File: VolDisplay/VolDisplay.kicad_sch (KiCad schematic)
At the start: 126 parts, among them J1 TYPE-C-31-M-12, SW1 PTS810_SJM_250_SMTR_LFS, SW2 PTS810_SJM_250_SMTR_LFS, U1 ESP32-S3-WROOM-1, U2 AMS1117-3.3

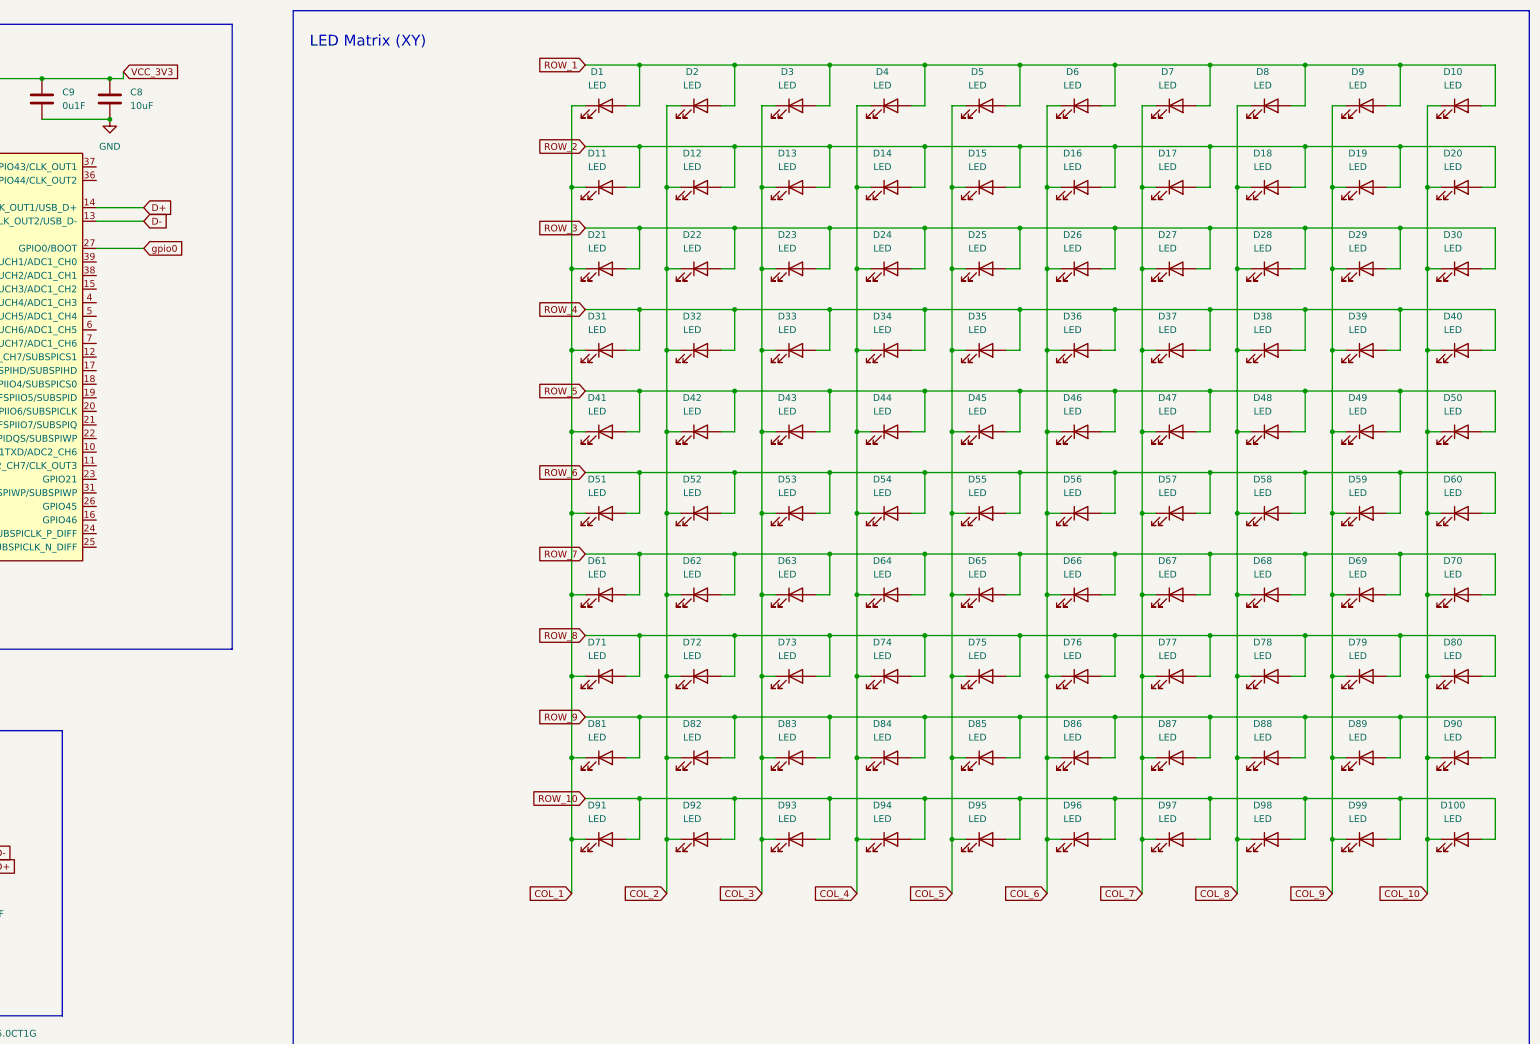
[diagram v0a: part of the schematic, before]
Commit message: Added the automation scripts we used, Schematic PDF is attached.
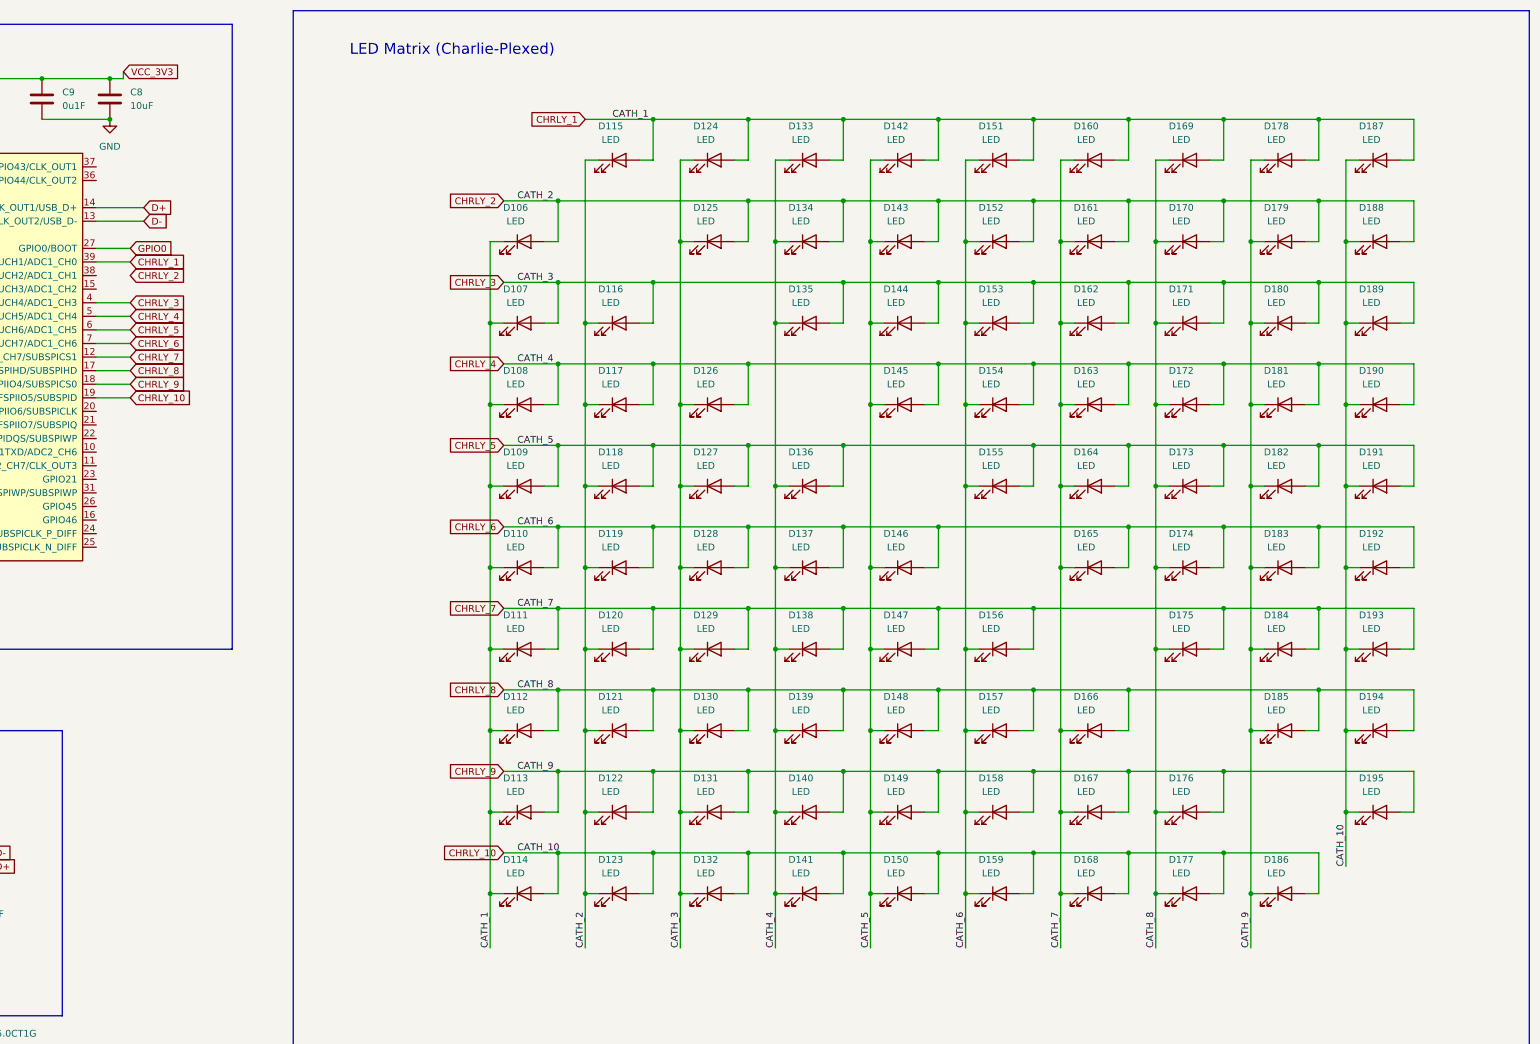
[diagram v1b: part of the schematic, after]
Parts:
- removed D1, D10, D100, D11, D12, D13, D14, D15, D16, D17, D18, D19, D2, D20, D21, D22, D23, D24, D25, D26, D27, D28, D29, D3, D30, D31, D32, D33, D34, D35, D36, D37, D38, D39, D4, D40, D41, D42, D43, D44, D45, D46, D47, D48, D49, D5, D50, D51, D52, D53, D54, D55, D56, D57, D58, D59, D6, D60, D61, D62, D63, D64, D65, D66, D67, D68, D69, D7, D70, D71, D72, D73, D74, D75, D76, D77, D78, D79, D8, D80, D81, D82, D83, D84, D85, D86, D87, D88, D89, D9, D90, D91, D92, D93, D94, D95, D96, D97, D98, D99: LED, LED_SMD:LED_0603_1608Metric_Pad1.05x0.95mm_HandSolder, symbol Device:LED
- added D106, D107, D108, D109, D110, D111, D112, D113, D114, D115, D116, D117, D118, D119, D120, D121, D122, D123, D124, D125, D126, D127, D128, D129, D130, D131, D132, D133, D134, D135, D136, D137, D138, D139, D140, D141, D142, D143, D144, D145, D146, D147, D148, D149, D150, D151, D152, D153, D154, D155, D156, D157, D158, D159, D160, D161, D162, D163, D164, D165, D166, D167, D168, D169, D170, D171, D172, D173, D174, D175, D176, D177, D178, D179, D180, D181, D182, D183, D184, D185, D186, D187, D188, D189, D190, D191, D192, D193, D194, D195: LED, LED_SMD:LED_0201_0603Metric, symbol Device:LED
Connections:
- net gpio0 is gone; now on net GPIO0: U1.27 (GPIO0/BOOT)
- net CHRLY_7: now reaches U1.12 (GPIO8/TOUCH8/ADC1_CH7/SUBSPICS1)
- net CHRLY_7: now also D111.2 (A), D120.2 (A), D129.2 (A), D138.2 (A), D147.2 (A), D156.2 (A), D160.1 (K), D161.1 (K), D162.1 (K), D163.1 (K), D164.1 (K), D165.1 (K), D166.1 (K), D167.1 (K), D168.1 (K), D175.2 (A), D184.2 (A), D193.2 (A)
- net CHRLY_8: now reaches U1.17 (GPIO9/TOUCH9/ADC1_CH8/FSPIHD/SUBSPIHD)
- net CHRLY_8: now also D112.2 (A), D121.2 (A), D130.2 (A), D139.2 (A), D148.2 (A), D157.2 (A), D166.2 (A), D169.1 (K), D170.1 (K), D171.1 (K), D172.1 (K), D173.1 (K), D174.1 (K), D175.1 (K), D176.1 (K), D177.1 (K), D185.2 (A), D194.2 (A)
- net CHRLY_9: now reaches U1.18 (GPIO10/TOUCH10/ADC1_CH9/FSPICS0/FSPIIO4/SUBSPICS0)
- net CHRLY_9: now also D113.2 (A), D122.2 (A), D131.2 (A), D140.2 (A), D149.2 (A), D158.2 (A), D167.2 (A), D176.2 (A), D178.1 (K), D179.1 (K), D180.1 (K), D181.1 (K), D182.1 (K), D183.1 (K), D184.1 (K), D185.1 (K), D186.1 (K), D195.2 (A)
- net CHRLY_10: now reaches U1.19 (GPIO11/TOUCH11/ADC2_CH0/FSPID/FSPIIO5/SUBSPID)
- net CHRLY_10: now also D114.2 (A), D123.2 (A), D132.2 (A), D141.2 (A), D150.2 (A), D159.2 (A), D168.2 (A), D177.2 (A), D186.2 (A), D187.1 (K), D188.1 (K), D189.1 (K), D190.1 (K), D191.1 (K), D192.1 (K), D193.1 (K), D194.1 (K), D195.1 (K)
- net CHRLY_1: now reaches U1.39 (GPIO1/TOUCH1/ADC1_CH0)
- net CHRLY_1: now also D106.1 (K), D107.1 (K), D108.1 (K), D109.1 (K), D110.1 (K), D111.1 (K), D112.1 (K), D113.1 (K), D114.1 (K), D115.2 (A), D124.2 (A), D133.2 (A), D142.2 (A), D151.2 (A), D160.2 (A), D169.2 (A), D178.2 (A), D187.2 (A)
- net CHRLY_3: now reaches U1.4 (GPIO4/TOUCH4/ADC1_CH3)
- net CHRLY_3: now also D107.2 (A), D116.2 (A), D124.1 (K), D125.1 (K), D126.1 (K), D127.1 (K), D128.1 (K), D129.1 (K), D130.1 (K), D131.1 (K), D132.1 (K), D135.2 (A), D144.2 (A), D153.2 (A), D162.2 (A), D171.2 (A), D180.2 (A), D189.2 (A)
- net CHRLY_4: now reaches U1.5 (GPIO5/TOUCH5/ADC1_CH4)
- net CHRLY_4: now also D108.2 (A), D117.2 (A), D126.2 (A), D133.1 (K), D134.1 (K), D135.1 (K), D136.1 (K), D137.1 (K), D138.1 (K), D139.1 (K), D140.1 (K), D141.1 (K), D145.2 (A), D154.2 (A), D163.2 (A), D172.2 (A), D181.2 (A), D190.2 (A)
- net CHRLY_5: now reaches U1.6 (GPIO6/TOUCH6/ADC1_CH5)
- net CHRLY_5: now also D109.2 (A), D118.2 (A), D127.2 (A), D136.2 (A), D142.1 (K), D143.1 (K), D144.1 (K), D145.1 (K), D146.1 (K), D147.1 (K), D148.1 (K), D149.1 (K), D150.1 (K), D155.2 (A), D164.2 (A), D173.2 (A), D182.2 (A), D191.2 (A)
- net CHRLY_6: now reaches U1.7 (GPIO7/TOUCH7/ADC1_CH6)
- net CHRLY_6: now also D110.2 (A), D119.2 (A), D128.2 (A), D137.2 (A), D146.2 (A), D151.1 (K), D152.1 (K), D153.1 (K), D154.1 (K), D155.1 (K), D156.1 (K), D157.1 (K), D158.1 (K), D159.1 (K), D165.2 (A), D174.2 (A), D183.2 (A), D192.2 (A)
- new net CHRLY_2: D106.2 (A), D115.1 (K), D116.1 (K), D117.1 (K), D118.1 (K), D119.1 (K), D120.1 (K), D121.1 (K), D122.1 (K), D123.1 (K), D125.2 (A), D134.2 (A), D143.2 (A), D152.2 (A), D161.2 (A), D170.2 (A), D179.2 (A), D188.2 (A)
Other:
- note added: "LED Matrix (Charlie-Plexed)"
- note removed: "LED Matrix (XY)"
- company: (none) -> Termin20
- title: (none) -> ESP32 LED Matrix
